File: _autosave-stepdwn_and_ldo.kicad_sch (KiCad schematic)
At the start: 21 parts

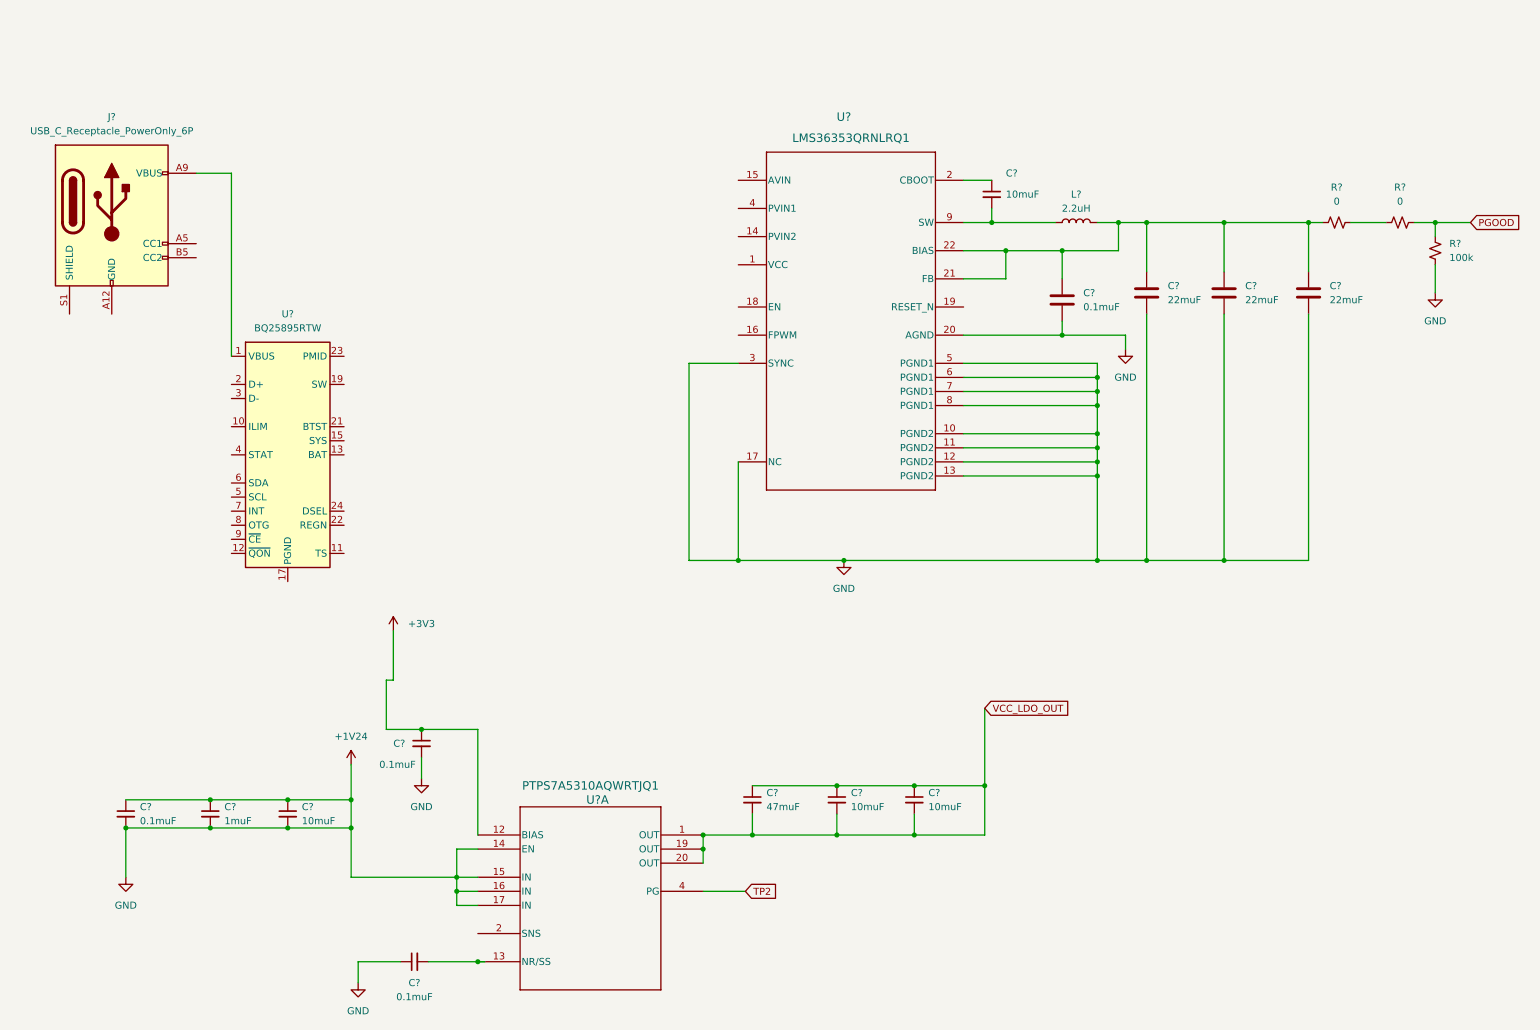
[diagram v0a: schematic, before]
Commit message: squasing ERC errors
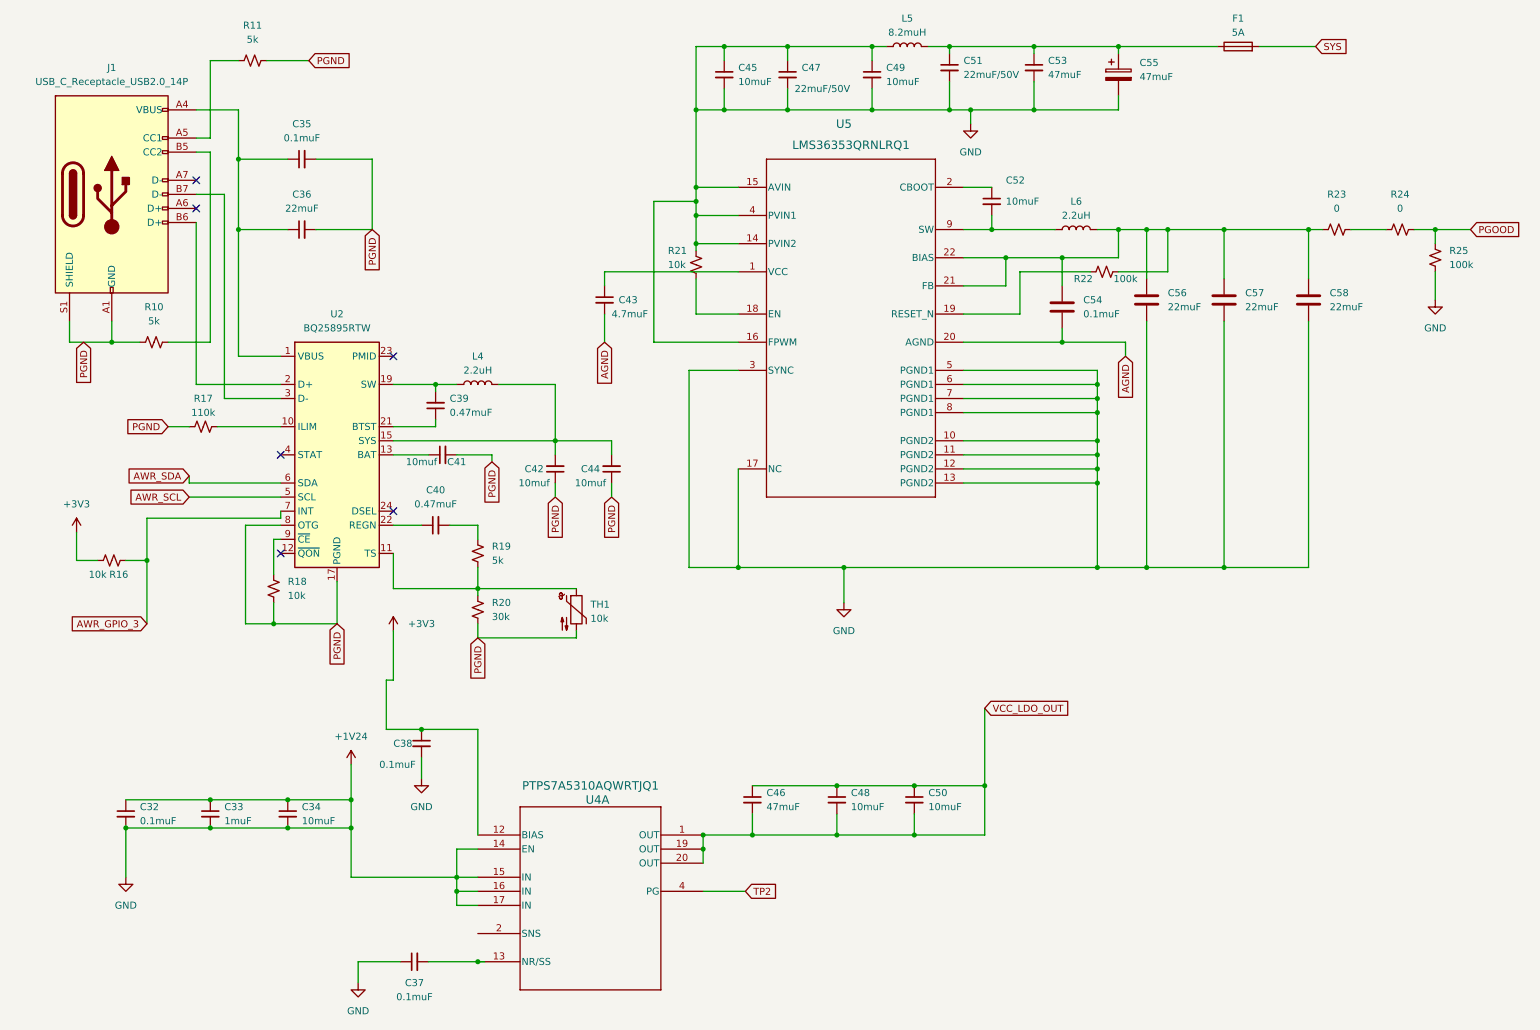
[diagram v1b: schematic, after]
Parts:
- removed J?: USB_C_Receptacle_PowerOnly_6P, symbol Connector:USB_C_Receptacle_PowerOnly_6P
- added C35: 0.1muF, symbol Device:C_Small
- added C36: 22muF, symbol Device:C_Small
- added C39, C40: 0.47muF, symbol Device:C_Small
- added C41, C42, C44: 10muf, symbol Device:C_Small
- added C43: 4.7muF, symbol Device:C_Small
- added C45, C49: 10muF, symbol Device:C_Small
- added C47, C51: 22muF/50V, symbol Device:C_Small
- added C53: 47muF, symbol Device:C_Small
- added C55: 47muF, symbol Device:C_Polarized
- added F1: 5A, symbol Device:Fuse
- added J1: USB_C_Receptacle_USB2.0_14P, symbol Connector:USB_C_Receptacle_USB2.0_14P
- added L4: 2.2uH, symbol Device:L
- added L5: 8.2muH, symbol Device:L
- added R10, R11, R19: 5k, symbol Device:R_Small_US
- added R16, R18, R21: 10k, symbol Device:R_Small_US
- added R17: 110k, symbol Device:R_Small_US
- added R20: 30k, symbol Device:R_Small_US
- added R22: 100k, symbol Device:R_Small_US
- added TH1: 10k, symbol Device:Thermistor_NTC
- gave numbers to parts that had none: 20
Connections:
- net +1V35: now also U5.14 (PVIN2), U5.15 (AVIN), U5.16 (FPWM), U5.4 (PVIN1), C45.1, C45.2, C47.1, C47.2, C49.1, C49.2, C51.2, C53.2, C55.2, L5.1, R21.1; no longer C54.2, U5.20 (AGND)
- net +3V3: now also R16.1
- net at C54.1, C56.1, C57.1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: now also R22.1
- net at U5.1 (VCC): now also C43.1
- net at U5.18 (EN): now also R21.2
- net at U5.19 (RESET_N): now also R22.2
- net at U2.1 (VBUS): now also C35.1, C36.1, J1.A4 (VBUS), J1.A9 (VBUS), J1.B4 (VBUS), J1.B9 (VBUS)
- net at U2.10 (ILIM): now also R17.2
- net at U2.11 (TS): now also R19.1, R20.2, TH1.1
- net at U2.13 (BAT), U2.14 (BAT): now also C41.1
- net at U2.15 (SYS), U2.16 (SYS): now also C42.2, C44.2, L4.2
- net PGND: now reaches U2.17 (PGND), U2.18 (PGND), U2.25 (PGND)
- net PGND: now also U2.8 (OTG), C35.2, C36.2, C41.2, C42.1, C44.1, J1.A1 (GND), J1.A12 (GND), J1.B1 (GND), J1.B12 (GND), J1.S1 (SHIELD), R10.1, R11.2, R17.1, R18.1, R20.1, TH1.2
- net at U2.19 (SW), U2.20 (SW): now also C39.2, L4.1
- net at U2.2 (D+): now also J1.B6 (D+)
- net at U2.21 (BTST): now also C39.1
- net at U2.22 (REGN): now also C40.1
- net at U2.3 (D-): now also J1.B7 (D-)
- net AWR_SCL: now reaches U2.5 (SCL)
- net AWR_SDA: now reaches U2.6 (SDA)
- net AWR_GPIO_3: now reaches U2.7 (INT)
- net AWR_GPIO_3: now also R16.2
- net at U2.9 (~{CE}): now also R18.2
- new net: C51.1, C53.1, C55.1, F1.1, L5.2
- new net: C40.2, R19.2
- new net: J1.B5 (CC2), R10.2
- new net: J1.A5 (CC1), R11.1
- new net AGND: C43.2, C54.2, U5.20 (AGND)
- new net SYS: F1.2
- no-connect marks 0 -> 6
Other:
- moved on the sheet: C52, C54, C56, C57, C58, L6, R23, R24, R25, U2, U5

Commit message: squased errors going over supply desgin
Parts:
- removed C41, C44: 10muf, symbol Device:C_Small
- added BT1: Battery, symbol Device:Battery
- added C5: 10muf, symbol Device:C_Small
- C42: value 10muf -> 22muf
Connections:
- net +1V35 is gone; now on net GND: C32.1, C32.2, C33.1, C33.2, C34.1, C34.2, C37.1, C38.2, C45.1, C45.2, C47.1, C47.2, C49.1, C49.2, C51.2, C53.2, C55.2, C56.2, C57.2, C58.2, L5.1, R21.1, R25.1, U4.14 (EN), U4.15 (IN), U4.16 (IN), U4.17 (IN), U5.10 (PGND2), U5.11 (PGND2), U5.12 (PGND2), U5.13 (PGND2), U5.14 (PVIN2), U5.15 (AVIN), U5.16 (FPWM), U5.17 (NC), U5.3 (SYNC), U5.4 (PVIN1), U5.5 (PGND1), U5.6 (PGND1), U5.7 (PGND1), U5.8 (PGND1)
- net VCC_LDO_OUT is gone; now on net GND: C46.1, C46.2, C48.1, C48.2, C50.1, C50.2, U4.1 (OUT), U4.19 (OUT), U4.20 (OUT)
- net +3V3: now also C54.1, C56.1, C57.1, C58.1, L6.2, R22.1, R23.1, U5.21 (FB), U5.22 (BIAS)
- net PGND: now also C5.2
- net at U2.13 (BAT), U2.14 (BAT): now also BT1.1 (+), C5.1
- net IN(TPS): now reaches C42.2, L4.2, U2.15 (SYS), U2.16 (SYS)
- net GND: now reaches U4.2 (SNS)
- net GND: now also BT1.2 (-)
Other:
- moved on the sheet: C42, C46

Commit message: some fixes
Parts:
- added C6: 8.2muF, symbol Device:C_Small
- added R28: 10k, symbol Device:R_Small_US
- C52: value 10muF -> 0.47muF
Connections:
- net PGND: now also C6.2; no longer U2.8 (OTG)
- net SYS: now also R28.1; no longer F1.2
- net AVIN (LMS): now reaches U2.23 (PMID)
- net AVIN (LMS): now also C6.1
- net IN(TPS): no longer names the net of C42.2, L4.2, U2.15 (SYS), U2.16 (SYS)
- new net: R28.2, U2.8 (OTG)
- new net PMID: F1.2
- no-connect marks 6 -> 5
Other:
- note added: "Find something for SYS (BQ)"
- note added: "VOUT"
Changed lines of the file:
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@@
 (kicad_sch (version 20230121) (generator eeschema)
   (paper "A4")
+  (junction (at 86.36 76.2) (diameter 0) (color 0 0 0 0)
+  )
   (junction (at 228.6 114.3) (diameter 0) (color 0 0 0 0)
   )
@@
   (junction (at 138.43 20.32) (diameter 0) (color 0 0 0 0)
   )
-  (junction (at 57.15 124.46) (diameter 0) (color 0 0 0 0)
-  )
   (junction (at 243.84 53.34) (diameter 0) (color 0 0 0 0)
   )
@@
   (junction (at 30.48 161.29) (diameter 0) (color 0 0 0 0)
   )
-  (junction (at 114.3 91.44) (diameter 0) (color 0 0 0 0)
-  )
   (junction (at 149.86 20.32) (diameter 0) (color 0 0 0 0)
   )
@@
   (junction (at 133.35 50.8) (diameter 0) (color 0 0 0 0)
   )
-  (no_connect (at 78.74 76.2))
   (no_connect (at 58.42 111.76))
   (no_connect (at 43.18 44.45))
@@
     (stroke (width 0) (type default))
   )
+  (wire (pts (xy 49.53 106.68) (xy 58.42 106.68))
+    (stroke (width 0) (type default))
+  )
   (wire (pts (xy 138.43 20.32) (xy 149.86 20.32))
     (stroke (width 0) (type default))
@@
     (stroke (width 0) (type default))
   )
+  (wire (pts (xy 86.36 76.2) (xy 86.36 71.12))
+    (stroke (width 0) (type default))
+  )
   (wire (pts (xy 189.23 63.5) (xy 189.23 58.42))
     (stroke (width 0) (type default))
@@
     (stroke (width 0) (type default))
   )
-  (wire (pts (xy 114.3 91.44) (xy 125.73 91.44))
-    (stroke (width 0) (type default))
-  )
   (wire (pts (xy 21.59 113.03) (xy 25.4 113.03))
     (stroke (width 0) (type default))
   )
+  (wire (pts (xy 45.72 119.38) (xy 45.72 127))
+    (stroke (width 0) (type default))
+  )
   (wire (pts (xy 205.74 91.44) (xy 205.74 93.98))
     (stroke (width 0) (type default))
@@
     (stroke (width 0) (type default))
   )
-  (wire (pts (xy 58.42 106.68) (xy 52.07 106.68))
+  (wire (pts (xy 49.53 109.22) (xy 45.72 109.22))
     (stroke (width 0) (type default))
   )
@@
     (stroke (width 0) (type default))
   )
+  (wire (pts (xy 90.17 72.39) (xy 100.33 72.39))
+    (stroke (width 0) (type default))
+  )
   (wire (pts (xy 74.93 53.34) (xy 74.93 40.64))
     (stroke (width 0) (type default))
   )
+  (wire (pts (xy 90.17 76.2) (xy 90.17 72.39))
+    (stroke (width 0) (type default))
+  )
   (wire (pts (xy 209.55 20.32) (xy 227.33 20.32))
     (stroke (width 0) (type default))
   )
+  (wire (pts (xy 86.36 76.2) (xy 90.17 76.2))
+    (stroke (width 0) (type default))
+  )
   (wire (pts (xy 72.39 185.42) (xy 72.39 189.23))
     (stroke (width 0) (type default))
@@
     (stroke (width 0) (type default))
   )
+  (wire (pts (xy 86.36 58.42) (xy 86.36 66.04))
+    (stroke (width 0) (type default))
+  )
   (wire (pts (xy 149.86 20.32) (xy 149.86 22.86))
     (stroke (width 0) (type default))
   )
-  (wire (pts (xy 52.07 124.46) (xy 57.15 124.46))
-    (stroke (width 0) (type default))
-  )
   (wire (pts (xy 243.84 53.34) (xy 246.38 53.34))
     (stroke (width 0) (type default))
@@
     (stroke (width 0) (type default))
   )
-  (wire (pts (xy 125.73 88.9) (xy 125.73 91.44))
-    (stroke (width 0) (type default))
-  )
   (wire (pts (xy 214.63 53.34) (xy 214.63 62.23))
     (stroke (width 0) (type default))
@@
     (stroke (width 0) (type default))
   )
+  (wire (pts (xy 100.33 72.39) (xy 100.33 69.85))
+    (stroke (width 0) (type default))
+  )
   (wire (pts (xy 181.61 73.66) (xy 199.39 73.66))
     (stroke (width 0) (type default))
@@
     (stroke (width 0) (type default))
   )
+  (wire (pts (xy 78.74 76.2) (xy 86.36 76.2))
+    (stroke (width 0) (type default))
+  )
   (wire (pts (xy 181.61 63.5) (xy 189.23 63.5))
     (stroke (width 0) (type default))
@@
     (stroke (width 0) (type default))
   )
-  (wire (pts (xy 52.07 106.68) (xy 52.07 124.46))
+  (wire (pts (xy 45.72 109.22) (xy 45.72 114.3))
     (stroke (width 0) (type default))
   )
@@
     (stroke (width 0) (type default))
   )
+  (wire (pts (xy 49.53 109.22) (xy 49.53 106.68))
+    (stroke (width 0) (type default))
+  )
   (wire (pts (xy 214.63 114.3) (xy 214.63 69.85))
     (stroke (width 0) (type default))
@@
     (stroke (width 0) (type default))
   )
-  (label "IN(TPS)" (at 125.73 88.9 0) (fields_autoplaced)
+  (text "Find something for SYS (BQ)" (at 92.71 90.17 0)
+    (effects (font (size 1.27 1.27)) (justify left bottom))
+  )
+  (text "VOUT\n" (at 237.49 40.64 0)
+    (effects (font (size 1.27 1.27)) (justify left bottom))
+  )
+  (label "AVIN (LMS)" (at 100.33 69.85 0) (fields_autoplaced)
+    (effects (font (size 1.27 1.27)) (justify left bottom))
+  )
+  (label "SYS" (at 45.72 127 0) (fields_autoplaced)
     (effects (font (size 1.27 1.27)) (justify left bottom))
   )
@@
     )
   )
-  (global_label "SYS" (shape input) (at 245.11 20.32 0) (fields_autoplaced)
+  (global_label "PMID" (shape input) (at 245.11 20.32 0) (fields_autoplaced)
     (effects (font (size 1.27 1.27)) (justify left))
-    (property "Intersheetrefs" "${INTERSHEET_REFS}" (at 251.6028 20.32 0)
+    (property "Intersheetrefs" "${INTERSHEET_REFS}" (at 252.6914 20.32 0)
       (effects (font (size 1.27 1.27)) (justify left) hide)
     )
@@
     (property "Intersheetrefs" "${INTERSHEET_REFS}" (at 22.86 81.7857 90)
       (effects (font (size 1.27 1.27)) (justify right) hide)
+    )
+  )
+  (global_label "PGND" (shape input) (at 86.36 58.42 90) (fields_autoplaced)
+    (effects (font (size 1.27 1.27)) (justify left))
+    (property "Intersheetrefs" "${INTERSHEET_REFS}" (at 86.36 50.2943 90)
+      (effects (font (size 1.27 1.27)) (justify left) hide)
     )
   )
@@
     )
   )
+  (symbol (lib_id "Device:R_Small_US") (at 45.72 116.84 180) (unit 1)
+    (in_bom yes) (on_board yes) (dnp no) (fields_autoplaced)
+    (property "Reference" "R28" (at 48.26 115.57 0)
+      (effects (font (size 1.27 1.27)) (justify right))
+    )
+    (property "Value" "10k" (at 48.26 118.11 0)
+      (effects (font (size 1.27 1.27)) (justify right))
+    )
+    (property "Footprint" "" (at 45.72 116.84 0)
+      (effects (font (size 1.27 1.27)) hide)
+    )
+    (property "Datasheet" "~" (at 45.72 116.84 0)
+      (effects (font (size 1.27 1.27)) hide)
+    )
+    (pin "2")
+    (pin "1")
+    (instances
+      (project "radar"
+        (path "/88b309aa-5f0e-45d7-beec-81d4b0ee2121/7a3c78f1-80f2-463b-a37f-9a7b3cc7f964/62900e5d-413e-4591-98ac-b12b6d69be62"
+          (reference "R28") (unit 1)
+        )
+      )
+    )
+  )
   (symbol (lib_id "Device:L") (at 93.98 81.28 90) (unit 1)
     (in_bom yes) (on_board yes) (dnp no) (fields_autoplaced)
@@
       (effects (font (size 1.27 1.27)) (justify left))
     )
-    (property "Value" "10muF" (at 189.23 48.26 0)
+    (property "Value" "0.47muF" (at 189.23 48.26 0)
       (effects (font (size 1.27 1.27)) (justify left))
     )
@@
         (path "/88b309aa-5f0e-45d7-beec-81d4b0ee2121/7a3c78f1-80f2-463b-a37f-9a7b3cc7f964/62900e5d-413e-4591-98ac-b12b6d69be62"
           (reference "U4") (unit 1)
+        )
+      )
+    )
+  )
+  (symbol (lib_id "Device:C_Small") (at 86.36 68.58 180) (unit 1)
+    (in_bom yes) (on_board yes) (dnp no) (fields_autoplaced)
+    (property "Reference" "C6" (at 88.9 67.3036 0)
+      (effects (font (size 1.27 1.27)) (justify right))
+    )
+    (property "Value" "8.2muF" (at 88.9 69.8436 0)
+      (effects (font (size 1.27 1.27)) (justify right))
+    )
+    (property "Footprint" "" (at 86.36 68.58 0)
+      (effects (font (size 1.27 1.27)) hide)
+    )
+    (property "Datasheet" "~" (at 86.36 68.58 0)
+      (effects (font (size 1.27 1.27)) hide)
+    )
+    (pin "2")
+    (pin "1")
+    (instances
+      (project "radar"
+        (path "/88b309aa-5f0e-45d7-beec-81d4b0ee2121/7a3c78f1-80f2-463b-a37f-9a7b3cc7f964/62900e5d-413e-4591-98ac-b12b6d69be62"
+          (reference "C6") (unit 1)
         )
       )
@@
     )
     (property "Value" "+3V3" (at 238.76 38.1 0)
-      (effects (font (size 1.27 1.27)))
+      (effects (font (size 1.27 1.27)) hide)
     )
     (property "Footprint" "" (at 238.76 43.18 0)

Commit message: making unit design for AWR1843, starting with GND, voltage, I2C and GPIO
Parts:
- removed R22, R25: 100k, symbol Device:R_Small_US
- removed R24: 0, symbol Device:R_Small_US
- added C7: 120muF, symbol Device:C_Polarized
- L6: value 2.2uH -> 10muH
- R23: value 0 -> 100k
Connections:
- net +3V3: now also R23.2, U4.14 (EN), C7.1; no longer R23.1
- net GND: now also C7.2; no longer U4.14 (EN)
- net AWR_RESET: now reaches U5.19 (RESET_N)
- net AWR_RESET: now also R23.1
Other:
- note added: "This may be renamed once reset pin on AWR is declared"
- moved on the sheet: C56, C57
